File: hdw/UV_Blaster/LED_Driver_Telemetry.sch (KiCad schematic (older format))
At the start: 11 parts

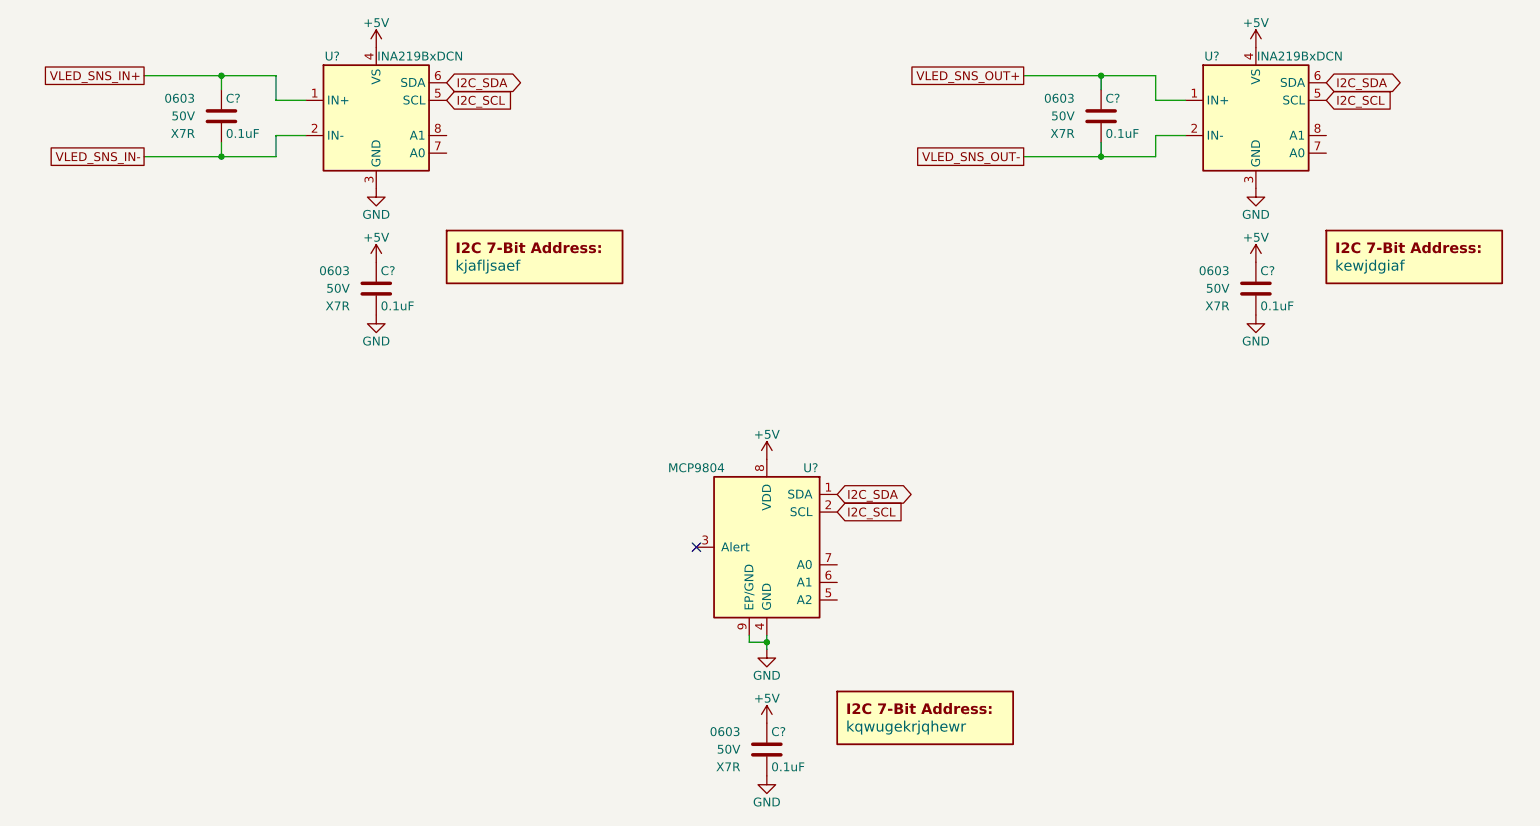
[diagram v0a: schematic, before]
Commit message: More sch work, netlist, part numbers, footprints
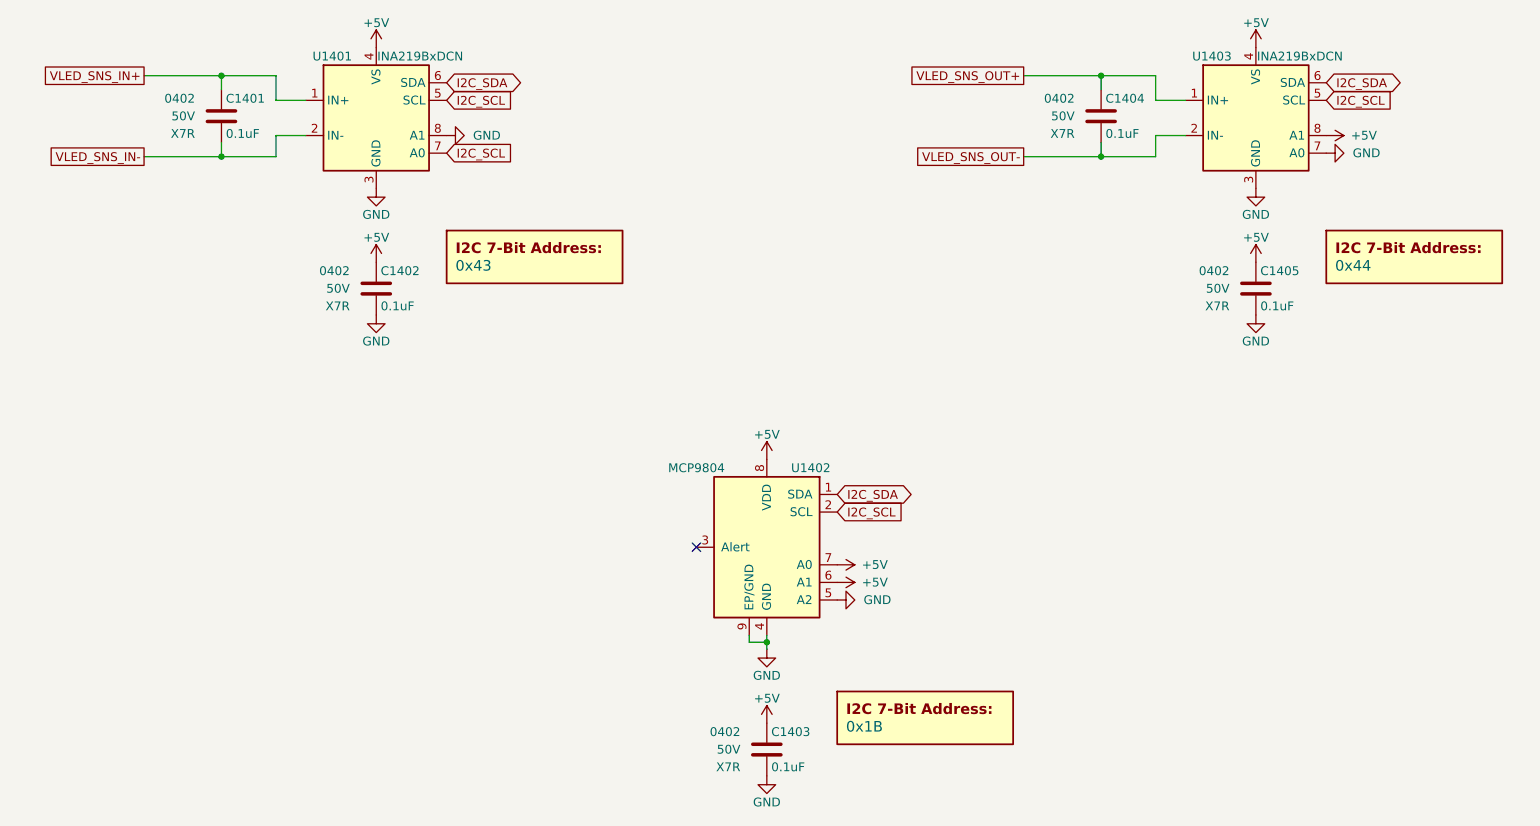
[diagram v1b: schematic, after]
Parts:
- removed DOC?: kewjdgiaf, symbol Custom_Library:I2C_Address
- removed DOC?: kjafljsaef, symbol Custom_Library:I2C_Address
- removed DOC?: kqwugekrjqhewr, symbol Custom_Library:I2C_Address
- added DOC1401: 0x43, symbol Custom_Library:I2C_Address
- added DOC1402: 0x1B, symbol Custom_Library:I2C_Address
- added DOC1403: 0x44, symbol Custom_Library:I2C_Address
- C1401, C1402, C1403, C1404, C1405: renamed from C?; footprint Capacitors_SMD:C_0603 -> Capacitors_SMD:C_0402; Configuration (none) -> Telemetry; Digi-Key PN 399-6856-1-ND -> 490-10701-1-ND; display_footprint 0603 -> 0402
- U1401, U1402, U1403: renamed from U?; Configuration (none) -> Telemetry
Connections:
- net +5V: now also U1402.6 (A1), U1402.7 (A0), U1403.8 (A1)
- net GND: now also U1401.8 (A1), U1402.5 (A2), U1403.7 (A0)
- net I2C_SCL: now also U1401.7 (A0)
